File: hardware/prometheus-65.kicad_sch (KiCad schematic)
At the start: 0 parts

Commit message: fix: fixed the footprint for the TMR2652D, added a 3d model, and linked it to the respective symbol
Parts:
- added U1: STM32F405RGTx, Package_QFP:LQFP-64_10x10mm_P0.5mm, symbol MCU_ST_STM32F4:STM32F405RGTx
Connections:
- new net: U1.18 (VSS), U1.63 (VSS)
- no-connect marks 0 -> 1
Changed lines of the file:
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@@
 	(generator_version "9.0")
 	(paper "A4")
+	(no_connect
+		(at 29.21 77.47)
+	)
+	(symbol
+		(lib_id "MCU_ST_STM32F4:STM32F405RGTx")
+		(at 44.45 69.85 0)
+		(unit 1)
+		(exclude_from_sim no)
+		(in_bom yes)
+		(on_board yes)
+		(dnp no)
+		(fields_autoplaced yes)
+		(property "Reference" "U1"
+			(at 49.1333 118.11 0)
+			(effects
+				(font
+					(size 1.27 1.27)
+				)
+				(justify left)
+			)
+		)
+		(property "Value" "STM32F405RGTx"
+			(at 49.1333 120.65 0)
+			(effects
+				(font
+					(size 1.27 1.27)
+				)
+				(justify left)
+			)
+		)
+		(property "Footprint" "Package_QFP:LQFP-64_10x10mm_P0.5mm"
+			(at 26.67 115.57 0)
+			(effects
+				(font
+					(size 1.27 1.27)
+				)
+				(justify right)
+				(hide yes)
+			)
+		)
+		(property "Datasheet" "https://www.st.com/resource/en/datasheet/stm32f405rg.pdf"
+			(at 44.45 69.85 0)
+			(effects
+				(font
+					(size 1.27 1.27)
+				)
+				(hide yes)
+			)
+		)
+		(property "Description" "STMicroelectronics Arm Cortex-M4 MCU, 1024KB flash, 192KB RAM, 168 MHz, 1.8-3.6V, 51 GPIO, LQFP64"
+			(at 44.45 69.85 0)
+			(effects
+				(font
+					(size 1.27 1.27)
+				)
+				(hide yes)
+			)
+		)
+		(pin "1"
+		)
+		(pin "5"
+		)
+		(pin "11"
+		)
+		(pin "8"
+		)
+		(pin "52"
+		)
+		(pin "32"
+		)
+		(pin "53"
+		)
+		(pin "60"
+		)
+		(pin "3"
+		)
+		(pin "40"
+		)
+		(pin "4"
+		)
+		(pin "19"
+		)
+		(pin "37"
+		)
+		(pin "39"
+		)
+		(pin "9"
+		)
+		(pin "51"
+		)
+		(pin "25"
+		)
+		(pin "47"
+		)
+		(pin "31"
+		)
+		(pin "7"
+		)
+		(pin "24"
+		)
+		(pin "10"
+		)
+		(pin "18"
+		)
+		(pin "63"
+		)
+		(pin "48"
+		)
+		(pin "12"
+		)
+		(pin "64"
+		)
+		(pin "13"
+		)
+		(pin "14"
+		)
+		(pin "15"
+		)
+		(pin "16"
+		)
+		(pin "17"
+		)
+		(pin "20"
+		)
+		(pin "21"
+		)
+		(pin "22"
+		)
+		(pin "23"
+		)
+		(pin "41"
+		)
+		(pin "42"
+		)
+		(pin "43"
+		)
+		(pin "44"
+		)
+		(pin "45"
+		)
+		(pin "46"
+		)
+		(pin "49"
+		)
+		(pin "50"
+		)
+		(pin "26"
+		)
+		(pin "27"
+		)
+		(pin "28"
+		)
+		(pin "55"
+		)
+		(pin "56"
+		)
+		(pin "57"
+		)
+		(pin "58"
+		)
+		(pin "59"
+		)
+		(pin "61"
+		)
+		(pin "62"
+		)
+		(pin "29"
+		)
+		(pin "30"
+		)
+		(pin "33"
+		)
+		(pin "34"
+		)
+		(pin "35"
+		)
+		(pin "36"
+		)
+		(pin "54"
+		)
+		(pin "38"
+		)
+		(pin "6"
+		)
+		(pin "2"
+		)
+		(instances
+			(project ""
+				(path "/7080535f-072d-4fc6-b033-a9cfe8594544"
+					(reference "U1")
+					(unit 1)
+				)
+			)
+		)
+	)
 	(sheet_instances
 		(path "/"

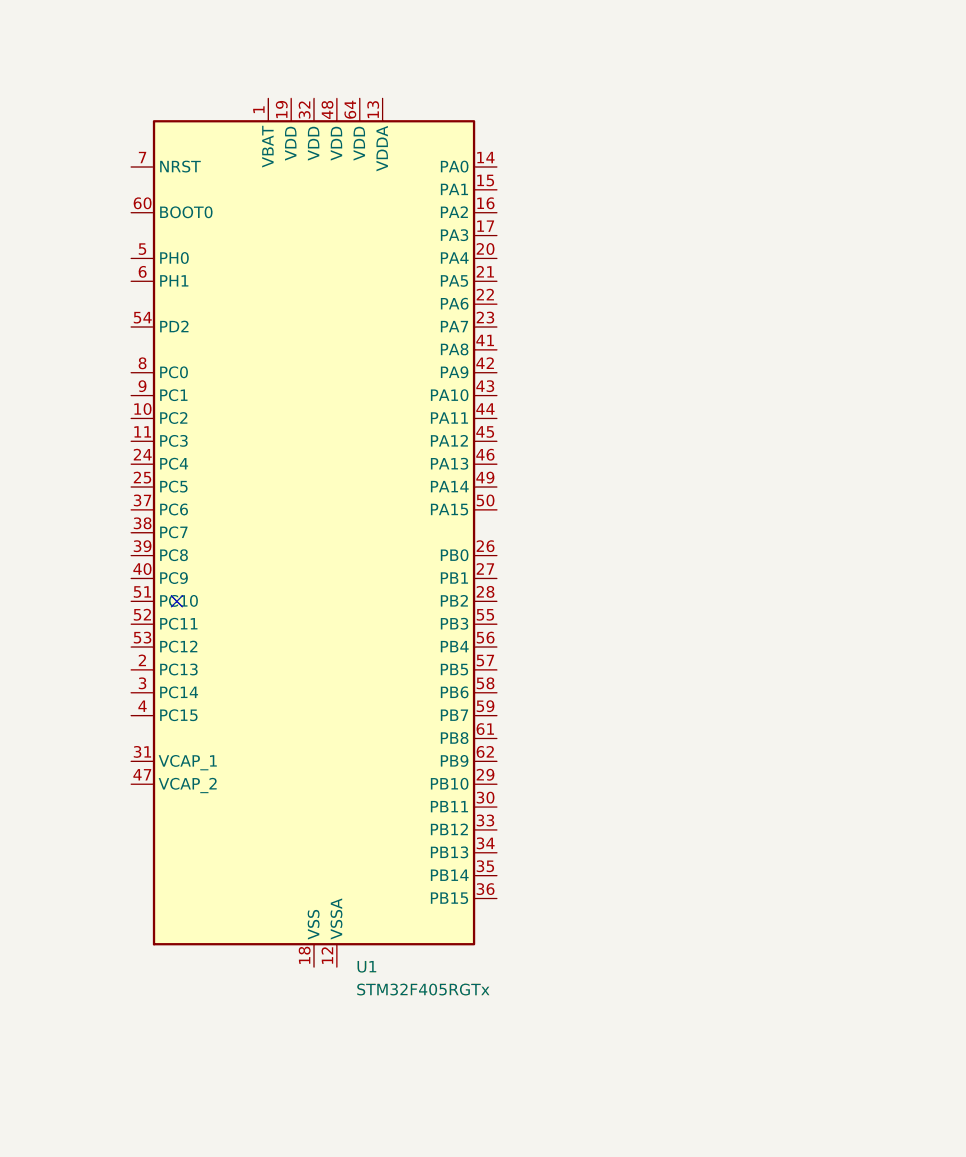
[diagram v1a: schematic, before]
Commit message: feat: started wiring the schematic, and added the STM32 datasheet
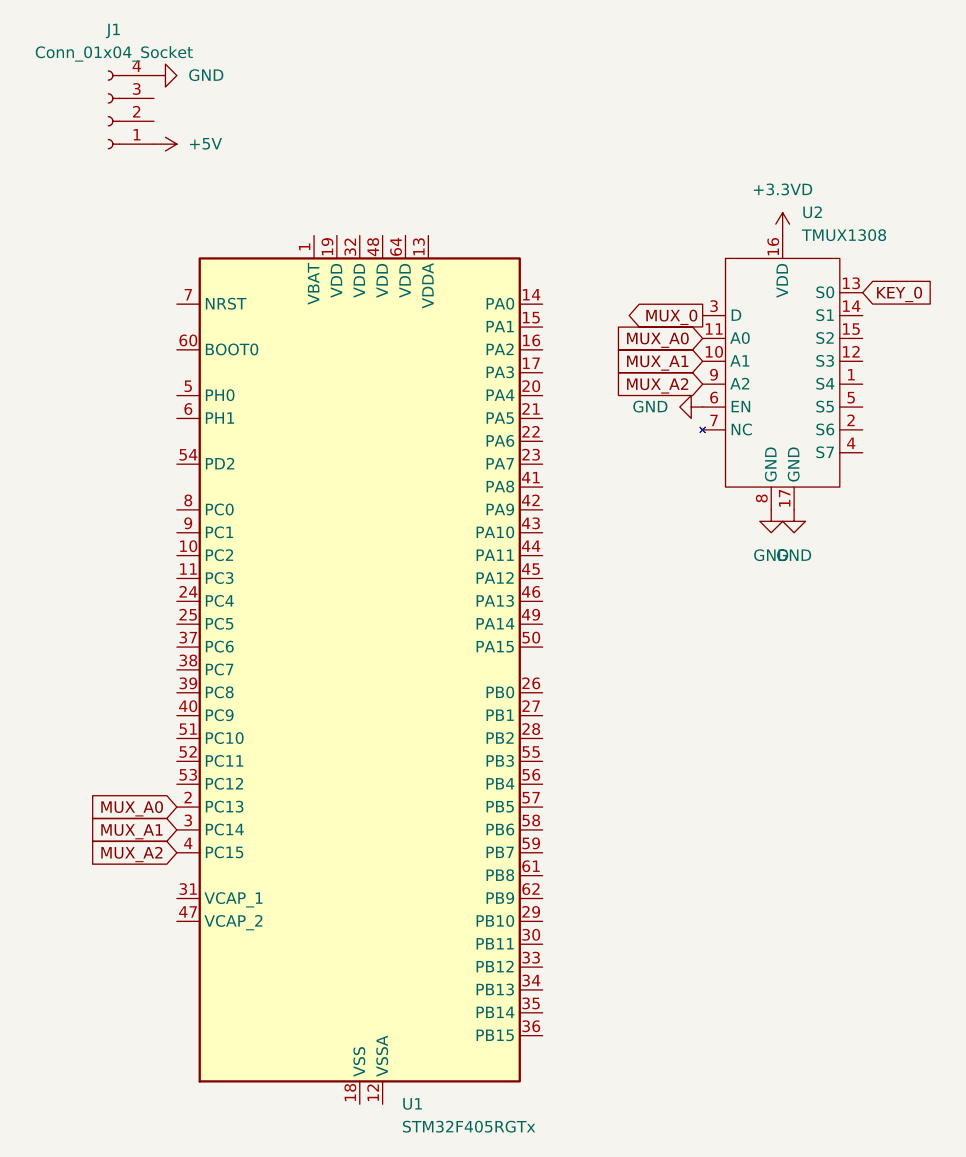
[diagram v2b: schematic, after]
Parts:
- added J1: Conn_01x04_Socket, symbol Connector:Conn_01x04_Socket
- added U2: TMUX1308, prometheus-65-footprints:QFN50P350X250X80-17N, symbol prometheus-65-symbols:TMUX1308
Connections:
- net MUX_A0: now reaches U1.2 (PC13)
- net MUX_A0: now also U2.11 (A0)
- net MUX_A1: now reaches U1.3 (PC14)
- net MUX_A1: now also U2.10 (A1)
- net MUX_A2: now reaches U1.4 (PC15)
- net MUX_A2: now also U2.9 (A2)
- new net +3.3VD: U2.16 (VDD)
- new net +5V: J1.1 (Pin_1)
- new net GND: J1.4 (Pin_4), U2.17 (GND), U2.6 (EN), U2.8 (GND)
- new net KEY_0: U2.13 (S0)
- new net MUX_0: U2.3 (D)
- no-connect marks 1 -> 0

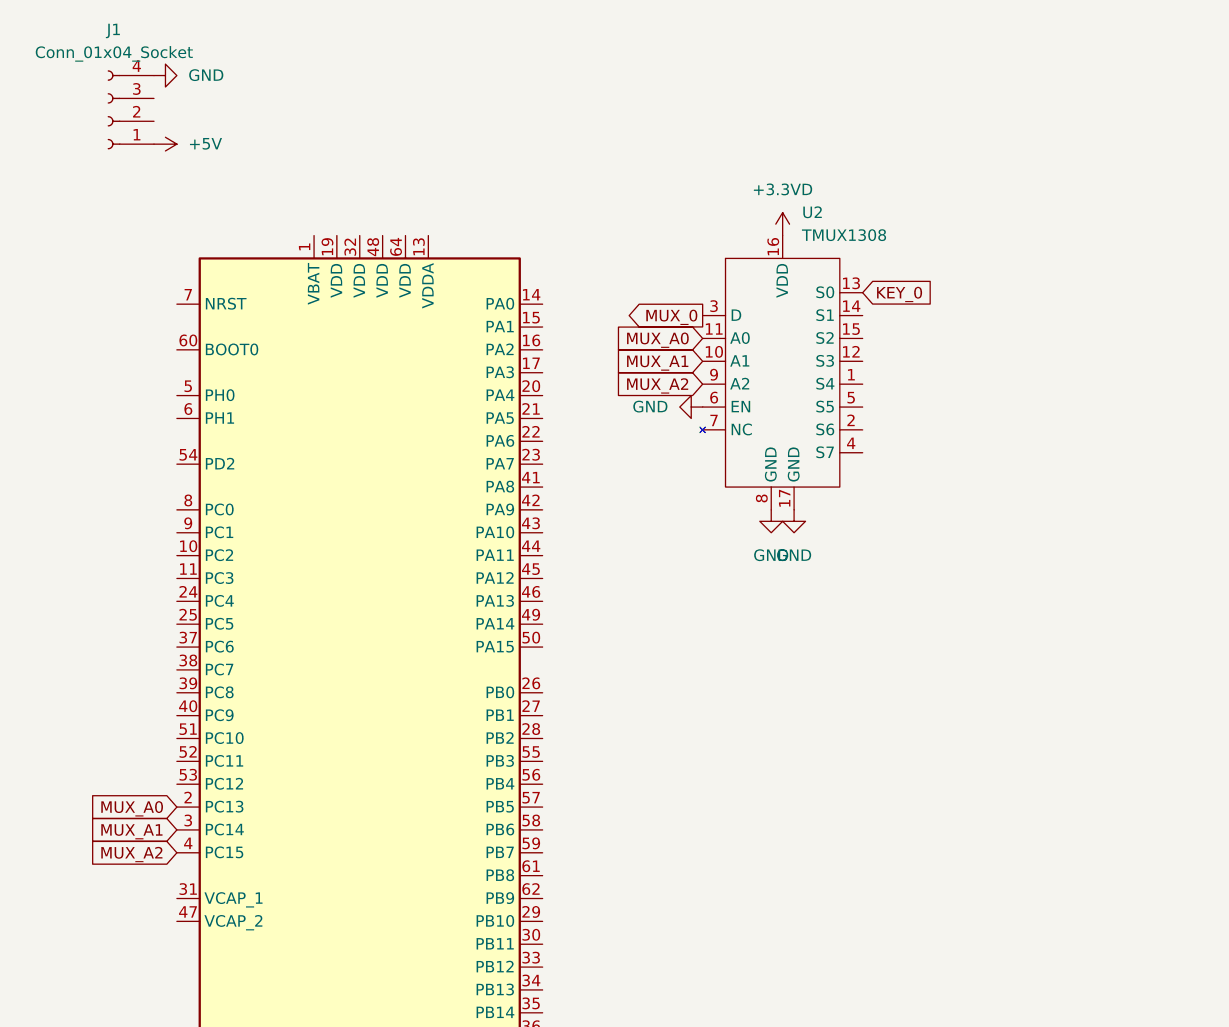
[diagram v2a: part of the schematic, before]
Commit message: fix: update duplicate label names, and fix directions
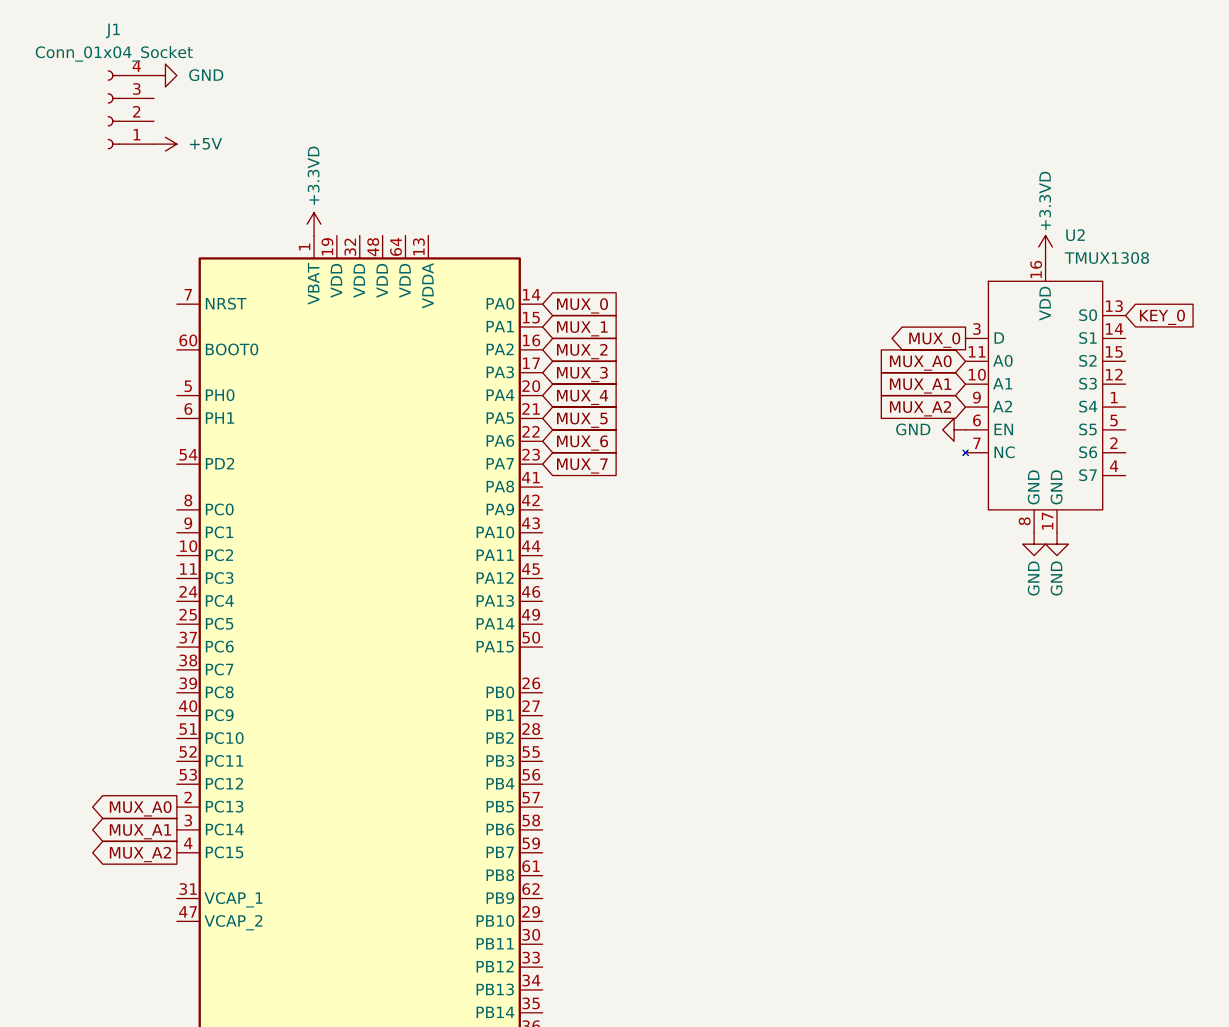
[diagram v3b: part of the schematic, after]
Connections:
- net +3.3VD: now also U1.1 (VBAT)
- net MUX_0: now also U1.14 (PA0)
- net MUX_1: now reaches U1.15 (PA1)
- net MUX_2: now reaches U1.16 (PA2)
- net MUX_3: now reaches U1.17 (PA3)
- net MUX_4: now reaches U1.20 (PA4)
- net MUX_5: now reaches U1.21 (PA5)
- net MUX_6: now reaches U1.22 (PA6)
- net MUX_7: now reaches U1.23 (PA7)
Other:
- moved on the sheet: U2
